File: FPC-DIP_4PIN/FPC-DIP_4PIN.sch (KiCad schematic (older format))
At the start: 2 parts, among them J1 Breadboard holes, J2 4 Pin FPC (1mm pitch)

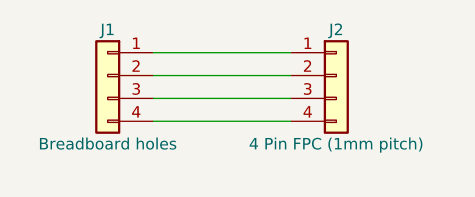
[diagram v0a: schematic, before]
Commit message: Fixed CTS PIN and added fpx sample mage from sensirion
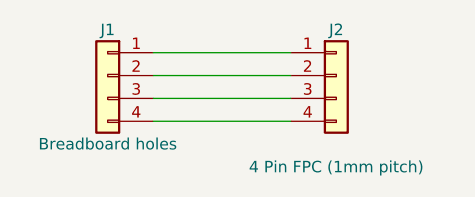
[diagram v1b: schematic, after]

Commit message: Added GND pad and labels for sensirion sample flex PCBs
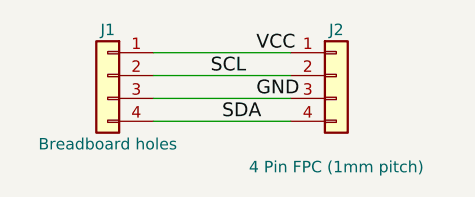
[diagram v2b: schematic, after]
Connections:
- net VCC: now reaches J1.1 (Pin_1), J2.1 (Pin_1)
- net SCL: now reaches J1.2 (Pin_2), J2.2 (Pin_2)
- net GND: now reaches J1.3 (Pin_3), J2.3 (Pin_3)
- net SDA: now reaches J1.4 (Pin_4), J2.4 (Pin_4)
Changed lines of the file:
@@
 Sheet 1 1
 Title "FPC to DIP Breadboard adapter"
-Date "2018-04-13"
-Rev "0.1"
+Date "2018-04-24"
+Rev "0.2"
 Comp "GDG Zürich"
 Comment1 "Usefull for Sensirion samples on Flex PCB"
@@
 EndData
 $EndBitmap
+Text Label 6050 3650 0    60   ~ 0
+VCC
+Text Label 5850 3750 0    60   ~ 0
+SCL
+Text Label 6050 3850 0    60   ~ 0
+GND
+Text Label 5900 3950 0    60   ~ 0
+SDA
 $EndSCHEMATC
